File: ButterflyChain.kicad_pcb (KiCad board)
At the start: 2 copper layers, 93.1 x 65.5 mm, 25 parts, among them J1 Input, J2 Output, J3 Antennae

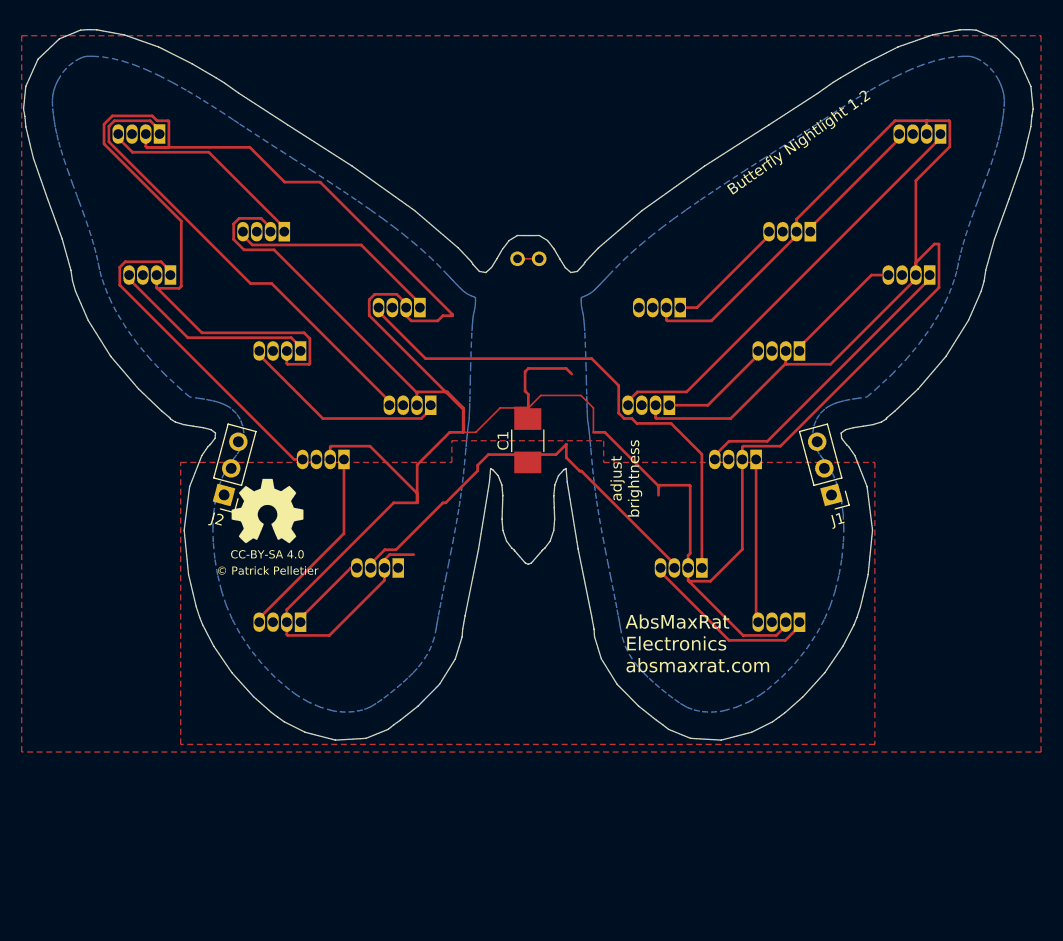
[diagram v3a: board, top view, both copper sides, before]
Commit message: Connect data in and out.
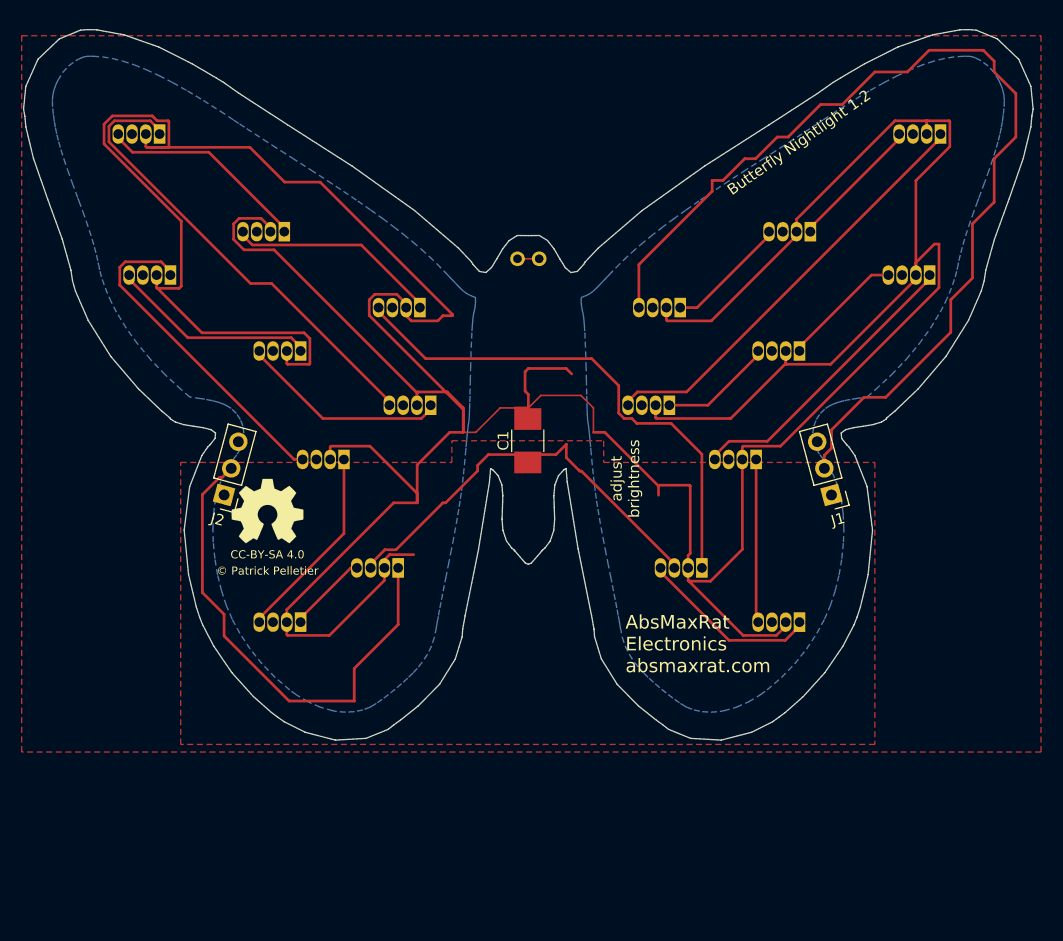
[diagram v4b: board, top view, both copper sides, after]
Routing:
- net Net-(D1-Pad4): track 0.36 -> 93.1 mm
- net Net-(D18-Pad1): track 0.00 -> 46.0 mm
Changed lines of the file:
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@@
     (thickness 1.6)
     (drawings 187)
-    (tracks 241)
+    (tracks 282)
     (zones 0)
     (modules 25)
@@
     (36 B.SilkS user)
     (37 F.SilkS user)
-    (38 B.Mask user)
+    (38 B.Mask user hide)
     (39 F.Mask user)
     (40 Dwgs.User user)
@@
   )
   (setup
-    (last_trace_width 0.1524)
+    (last_trace_width 0.254)
     (user_trace_width 0.254)
     (user_trace_width 0.508)
@@
     (pad_to_mask_clearance 0)
     (aux_axis_origin 0 0)
-    (visible_elements FFFEF77F)
+    (visible_elements FFFEE77F)
     (pcbplotparams
       (layerselection 0x010f0_80000001)
@@
   (segment (start 115.608006 98.72564) (end 122.243006 92.09064) (width 0.25) (layer F.Cu) (net 3) (status 20))
   (segment (start 122.243006 92.09064) (end 122.243006 91.72564) (width 0.25) (layer F.Cu) (net 3) (status 30))
+  (segment (start 117 88) (end 110.243006 94.756994) (width 0.254) (layer F.Cu) (net 4))
+  (segment (start 110.243006 94.756994) (end 110.243006 98.72564) (width 0.254) (layer F.Cu) (net 4))
+  (segment (start 117 87) (end 117 88) (width 0.254) (layer F.Cu) (net 4))
+  (segment (start 118 87) (end 117 87) (width 0.254) (layer F.Cu) (net 4))
+  (segment (start 120 85) (end 118 87) (width 0.254) (layer F.Cu) (net 4))
+  (segment (start 121 85) (end 120 85) (width 0.254) (layer F.Cu) (net 4))
+  (segment (start 123 83) (end 121 85) (width 0.254) (layer F.Cu) (net 4))
+  (segment (start 124 83) (end 123 83) (width 0.254) (layer F.Cu) (net 4))
+  (segment (start 127 80) (end 124 83) (width 0.254) (layer F.Cu) (net 4))
+  (segment (start 129 80) (end 127 80) (width 0.254) (layer F.Cu) (net 4))
+  (segment (start 132 77) (end 129 80) (width 0.254) (layer F.Cu) (net 4))
+  (segment (start 135 77) (end 132 77) (width 0.254) (layer F.Cu) (net 4))
+  (segment (start 137 75) (end 135 77) (width 0.254) (layer F.Cu) (net 4))
+  (segment (start 142 75) (end 137 75) (width 0.254) (layer F.Cu) (net 4))
+  (segment (start 143 76) (end 142 75) (width 0.254) (layer F.Cu) (net 4))
+  (segment (start 143 77) (end 143 76) (width 0.254) (layer F.Cu) (net 4))
+  (segment (start 145 79) (end 143 77) (width 0.254) (layer F.Cu) (net 4))
+  (segment (start 145 83) (end 145 79) (width 0.254) (layer F.Cu) (net 4))
+  (segment (start 143 85) (end 145 83) (width 0.254) (layer F.Cu) (net 4))
+  (segment (start 143 89) (end 143 85) (width 0.254) (layer F.Cu) (net 4))
+  (segment (start 141 91) (end 143 89) (width 0.254) (layer F.Cu) (net 4))
+  (segment (start 141 96) (end 141 91) (width 0.254) (layer F.Cu) (net 4))
+  (segment (start 139 98) (end 141 96) (width 0.254) (layer F.Cu) (net 4))
+  (segment (start 139 101) (end 139 98) (width 0.254) (layer F.Cu) (net 4))
+  (segment (start 133 107) (end 139 101) (width 0.254) (layer F.Cu) (net 4))
+  (segment (start 131 107) (end 133 107) (width 0.254) (layer F.Cu) (net 4))
+  (segment (start 128 110) (end 131 107) (width 0.254) (layer F.Cu) (net 4))
+  (segment (start 128 111.687067) (end 128 110) (width 0.254) (layer F.Cu) (net 4))
+  (segment (start 127.3426 113.546548) (end 127.3426 112.344467) (width 0.254) (layer F.Cu) (net 4))
+  (segment (start 127.3426 112.344467) (end 128 111.687067) (width 0.254) (layer F.Cu) (net 4))
   (segment (start 110.243006 98.36064) (end 110.243006 98.72564) (width 0.25) (layer F.Cu) (net 4) (status 30))
   (segment (start 126.053006 91.72564) (end 126.053006 91.36064) (width 0.25) (layer F.Cu) (net 5) (status 30))
@@
   (segment (start 83.688006 122.72564) (end 84.243006 122.72564) (width 0.25) (layer F.Cu) (net 20) (status 20))
   (segment (start 79.053006 127.36064) (end 83.688006 122.72564) (width 0.25) (layer F.Cu) (net 20) (status 10))
+  (segment (start 72.6574 113.546548) (end 71.807401 114.396547) (width 0.254) (layer F.Cu) (net 21))
+  (segment (start 70 125) (end 72 127) (width 0.254) (layer F.Cu) (net 21))
+  (segment (start 88.053006 127.946994) (end 88.053006 122.72564) (width 0.254) (layer F.Cu) (net 21))
+  (segment (start 71.807401 114.396547) (end 71.566231 114.396547) (width 0.254) (layer F.Cu) (net 21))
+  (segment (start 71.566231 114.396547) (end 70 115.962778) (width 0.254) (layer F.Cu) (net 21))
+  (segment (start 72 129) (end 78 135) (width 0.254) (layer F.Cu) (net 21))
+  (segment (start 70 115.962778) (end 70 125) (width 0.254) (layer F.Cu) (net 21))
+  (segment (start 84 132) (end 88.053006 127.946994) (width 0.254) (layer F.Cu) (net 21))
+  (segment (start 72 127) (end 72 129) (width 0.254) (layer F.Cu) (net 21))
+  (segment (start 78 135) (end 84 135) (width 0.254) (layer F.Cu) (net 21))
+  (segment (start 84 135) (end 84 132) (width 0.254) (layer F.Cu) (net 21))
   (segment (start 101.053006 94.22564) (end 99.053006 94.22564) (width 0.1524) (layer F.Cu) (net 22) (status 30))
   (zone (net 1) (net_name +5V) (layer B.Cu) (hatch edge 0.508)

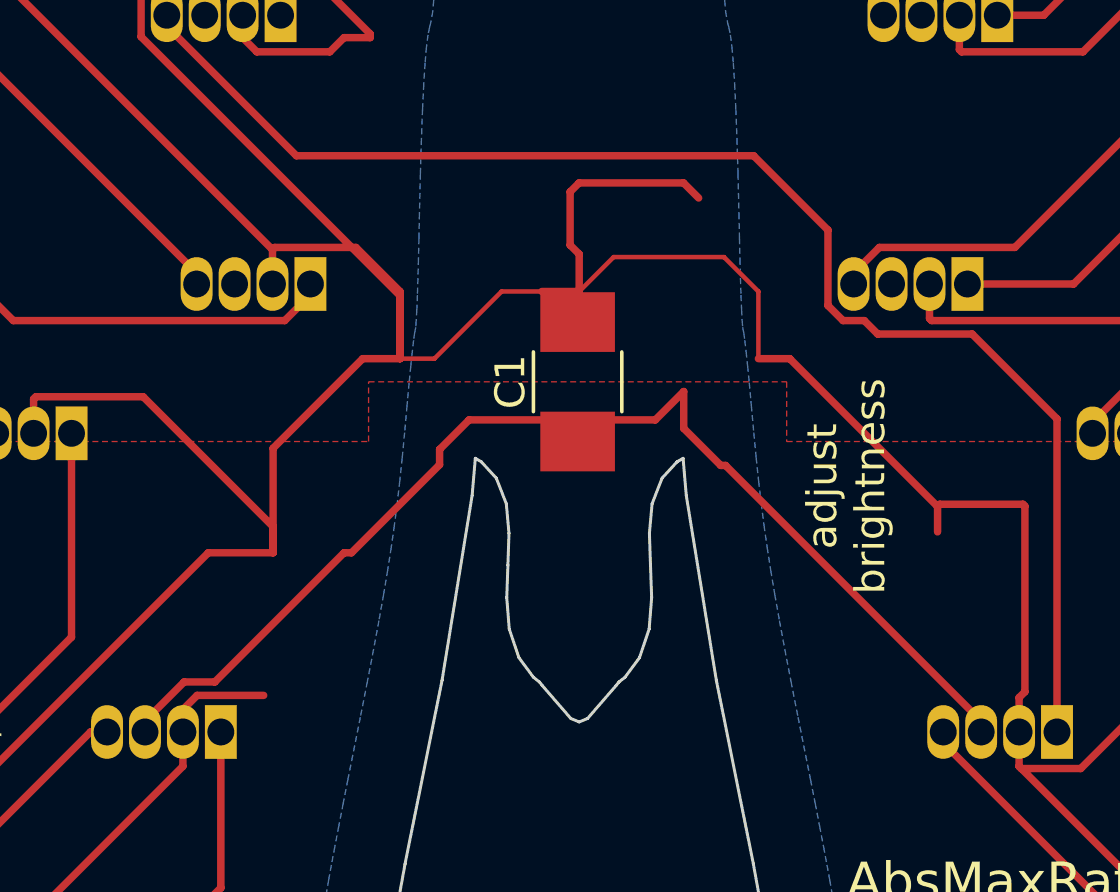
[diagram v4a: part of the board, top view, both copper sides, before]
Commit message: Fill zones.
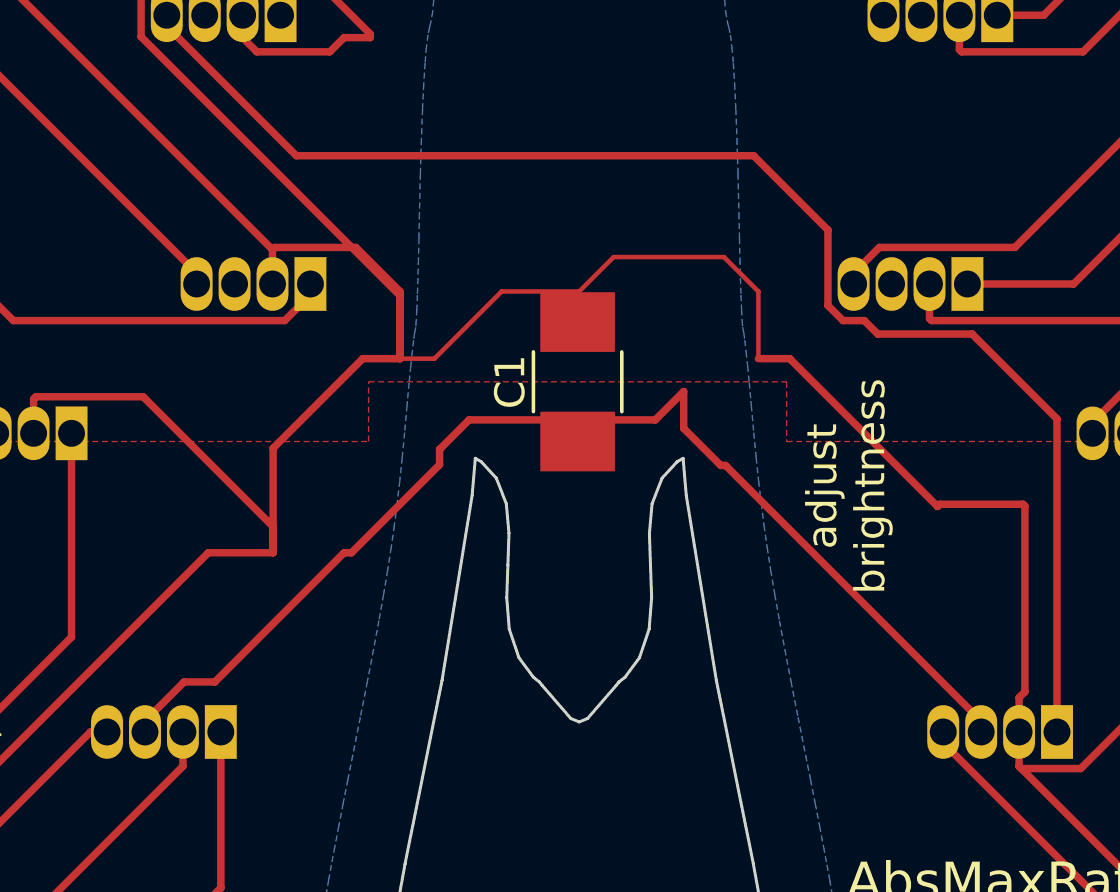
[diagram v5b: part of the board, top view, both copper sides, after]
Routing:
- net GND: track 398.5 -> 385.4 mm
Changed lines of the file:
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@@
   (general
     (links 60)
-    (no_connects 7)
+    (no_connects 0)
     (area 53.462159 73.047739 146.643853 138.651281)
     (thickness 1.6)
     (drawings 187)
-    (tracks 282)
+    (tracks 272)
     (zones 0)
     (modules 25)
@@
   (segment (start 113.513006 122.36064) (end 113.513006 122.72564) (width 0.25) (layer F.Cu) (net 1) (status 30))
   (segment (start 111.513006 99.09064) (end 111.513006 98.72564) (width 0.25) (layer F.Cu) (net 1) (status 30))
-  (segment (start 100.04938 104.340159) (end 99.749132 104.640407) (width 0.25) (layer F.Cu) (net 2))
-  (segment (start 104.053006 104.84564) (end 103.547525 104.340159) (width 0.25) (layer F.Cu) (net 2))
-  (segment (start 103.547525 104.340159) (end 100.04938 104.340159) (width 0.25) (layer F.Cu) (net 2))
-  (segment (start 99.749132 106.421766) (end 100.053006 106.72564) (width 0.25) (layer F.Cu) (net 2))
-  (segment (start 99.749132 104.640407) (end 99.749132 106.421766) (width 0.25) (layer F.Cu) (net 2))
-  (segment (start 100.053006 106.72564) (end 100.053006 107.97564) (width 0.25) (layer F.Cu) (net 2))
   (segment (start 74.378719 83.950641) (end 64.858007 83.950641) (width 0.25) (layer F.Cu) (net 2))
   (segment (start 77.582488 87.154411) (end 74.378719 83.950641) (width 0.25) (layer F.Cu) (net 2))
-  (segment (start 93.053006 99.47564) (end 93.053006 99.35064) (width 0.25) (layer F.Cu) (net 2) (status 30))
+  (segment (start 93.053006 99.47564) (end 93.053006 99.35064) (width 0.25) (layer F.Cu) (net 2))
   (segment (start 80.856777 87.154411) (end 77.582488 87.154411) (width 0.25) (layer F.Cu) (net 2))
-  (segment (start 93.053006 99.35064) (end 80.856777 87.154411) (width 0.25) (layer F.Cu) (net 2) (status 10))
+  (segment (start 93.053006 99.35064) (end 80.856777 87.154411) (width 0.25) (layer F.Cu) (net 2))
   (segment (start 112.053006 115.17564) (end 107.103006 110.22564) (width 0.25) (layer F.Cu) (net 2))
-  (segment (start 89.488009 121.500639) (end 87.258005 121.500639) (width 0.25) (layer F.Cu) (net 2))
-  (segment (start 87.258005 121.500639) (end 86.783006 121.975638) (width 0.25) (layer F.Cu) (net 2) (status 20))
   (segment (start 86.783006 121.975638) (end 86.783006 122.72564) (width 0.25) (layer F.Cu) (net 2) (status 30))
   (segment (start 100.053006 107.97564) (end 97.455406 107.97564) (width 0.1524) (layer F.Cu) (net 2))
@@
   (segment (start 114.913007 115.100639) (end 112.128007 115.100639) (width 0.25) (layer F.Cu) (net 2))
   (segment (start 112.128007 115.100639) (end 112.053006 115.17564) (width 0.25) (layer F.Cu) (net 2))
-  (segment (start 112.053006 116.02564) (end 112.053006 115.17564) (width 0.25) (layer F.Cu) (net 2))
   (segment (start 107.103006 110.22564) (end 106.053006 110.22564) (width 0.25) (layer F.Cu) (net 2))
   (segment (start 77.783006 127.72564) (end 77.783006 126.57564) (width 0.25) (layer F.Cu) (net 2) (status 10))
@@
   (segment (start 89.803006 113.22564) (end 92.803006 110.22564) (width 0.25) (layer F.Cu) (net 2))
   (segment (start 92.803006 110.22564) (end 94.053006 110.22564) (width 0.25) (layer F.Cu) (net 2))
-  (segment (start 98.803006 107.97564) (end 100.053006 107.97564) (width 0.25) (layer F.Cu) (net 2))
-  (segment (start 93.053006 99.47564) (end 92.178006 99.47564) (width 0.25) (layer F.Cu) (net 2) (status 30))
-  (segment (start 92.178006 99.47564) (end 91.703005 99.950641) (width 0.25) (layer F.Cu) (net 2) (status 10))
+  (segment (start 93.053006 99.47564) (end 92.178006 99.47564) (width 0.25) (layer F.Cu) (net 2))
+  (segment (start 92.178006 99.47564) (end 91.703005 99.950641) (width 0.25) (layer F.Cu) (net 2))
   (segment (start 91.703005 99.950641) (end 89.258005 99.950641) (width 0.25) (layer F.Cu) (net 2))
   (segment (start 89.258005 99.950641) (end 88.783006 99.475642) (width 0.25) (layer F.Cu) (net 2) (status 20))
@@
   (segment (start 122.243006 92.09064) (end 122.243006 91.72564) (width 0.25) (layer F.Cu) (net 3) (status 30))
   (segment (start 117 88) (end 110.243006 94.756994) (width 0.254) (layer F.Cu) (net 4))
-  (segment (start 110.243006 94.756994) (end 110.243006 98.72564) (width 0.254) (layer F.Cu) (net 4))
+  (segment (start 110.243006 94.756994) (end 110.243006 98.72564) (width 0.254) (layer F.Cu) (net 4) (status 20))
   (segment (start 117 87) (end 117 88) (width 0.254) (layer F.Cu) (net 4))
   (segment (start 118 87) (end 117 87) (width 0.254) (layer F.Cu) (net 4))
@@
   (segment (start 128 110) (end 131 107) (width 0.254) (layer F.Cu) (net 4))
   (segment (start 128 111.687067) (end 128 110) (width 0.254) (layer F.Cu) (net 4))
-  (segment (start 127.3426 113.546548) (end 127.3426 112.344467) (width 0.254) (layer F.Cu) (net 4))
+  (segment (start 127.3426 113.546548) (end 127.3426 112.344467) (width 0.254) (layer F.Cu) (net 4) (status 10))
   (segment (start 127.3426 112.344467) (end 128 111.687067) (width 0.254) (layer F.Cu) (net 4))
   (segment (start 110.243006 98.36064) (end 110.243006 98.72564) (width 0.25) (layer F.Cu) (net 4) (status 30))
@@
   (segment (start 83.688006 122.72564) (end 84.243006 122.72564) (width 0.25) (layer F.Cu) (net 20) (status 20))
   (segment (start 79.053006 127.36064) (end 83.688006 122.72564) (width 0.25) (layer F.Cu) (net 20) (status 10))
-  (segment (start 72.6574 113.546548) (end 71.807401 114.396547) (width 0.254) (layer F.Cu) (net 21))
+  (segment (start 72.6574 113.546548) (end 71.807401 114.396547) (width 0.254) (layer F.Cu) (net 21) (status 10))
   (segment (start 70 125) (end 72 127) (width 0.254) (layer F.Cu) (net 21))
-  (segment (start 88.053006 127.946994) (end 88.053006 122.72564) (width 0.254) (layer F.Cu) (net 21))
+  (segment (start 88.053006 127.946994) (end 88.053006 122.72564) (width 0.254) (layer F.Cu) (net 21) (status 20))
   (segment (start 71.807401 114.396547) (end 71.566231 114.396547) (width 0.254) (layer F.Cu) (net 21))
   (segment (start 71.566231 114.396547) (end 70 115.962778) (width 0.254) (layer F.Cu) (net 21))
@@
     (connect_pads (clearance 0.3048))
     (min_thickness 0.254)
-    (fill (arc_segments 16) (thermal_gap 0.508) (thermal_bridge_width 0.508))
+    (fill yes (arc_segments 16) (thermal_gap 0.508) (thermal_bridge_width 0.508))
     (polygon
       (pts
@@
     (connect_pads (clearance 0.3048))
     (min_thickness 0.254)
-    (fill (arc_segments 16) (thermal_gap 0.508) (thermal_bridge_width 0.508))
+    (fill yes (arc_segments 16) (thermal_gap 0.508) (thermal_bridge_width 0.508))
     (polygon
       (pts
